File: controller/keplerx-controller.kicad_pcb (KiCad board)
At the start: 2 copper layers, 90 x 50 mm, 21 parts, among them J1 Conn_02x05_Odd_Even, J2 Conn_01x04, J3 Conn_01x04, SW1 Synth, SW2 ROM, SW3 Vol-, SW4 Vol+, SW5 RotaryEncoder_Switch

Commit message: 再再度出し直し(v2.0.2)
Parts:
- added H5: MountingHole_Pad, MountingHole:MountingHole_2.2mm_M2_ISO7380_Pad, F.Cu at (124.5, 99.5)
- added H6: MountingHole_Pad, MountingHole:MountingHole_2.2mm_M2_ISO7380_Pad, F.Cu at (124.5, 77.5)
- added H7: MountingHole_Pad, MountingHole:MountingHole_2.2mm_M2_ISO7380_Pad, F.Cu at (145.5, 99.5)
- added H8: MountingHole_Pad, MountingHole:MountingHole_2.2mm_M2_ISO7380_Pad, F.Cu at (145.5, 77.5)
- moved JP1 0.29 mm to (130.8, 73.3)
- moved JP4 0.24 mm to (130.8, 80.6)
- moved JP2 0.22 mm to (134.0, 73.3)
- moved JP3 0.15 mm to (134.0, 80.6)
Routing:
- net /BTN4: track 57.9 -> 56.4 mm
- net Net-(J3-Pad4): track 5.85 -> 5.33 mm
- net (no net): vias 4 -> 0
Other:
- board text added: "Developed by @kunichiko. January 2023 (V1.0.0)"
- board text added: "Kepler-X Controller"

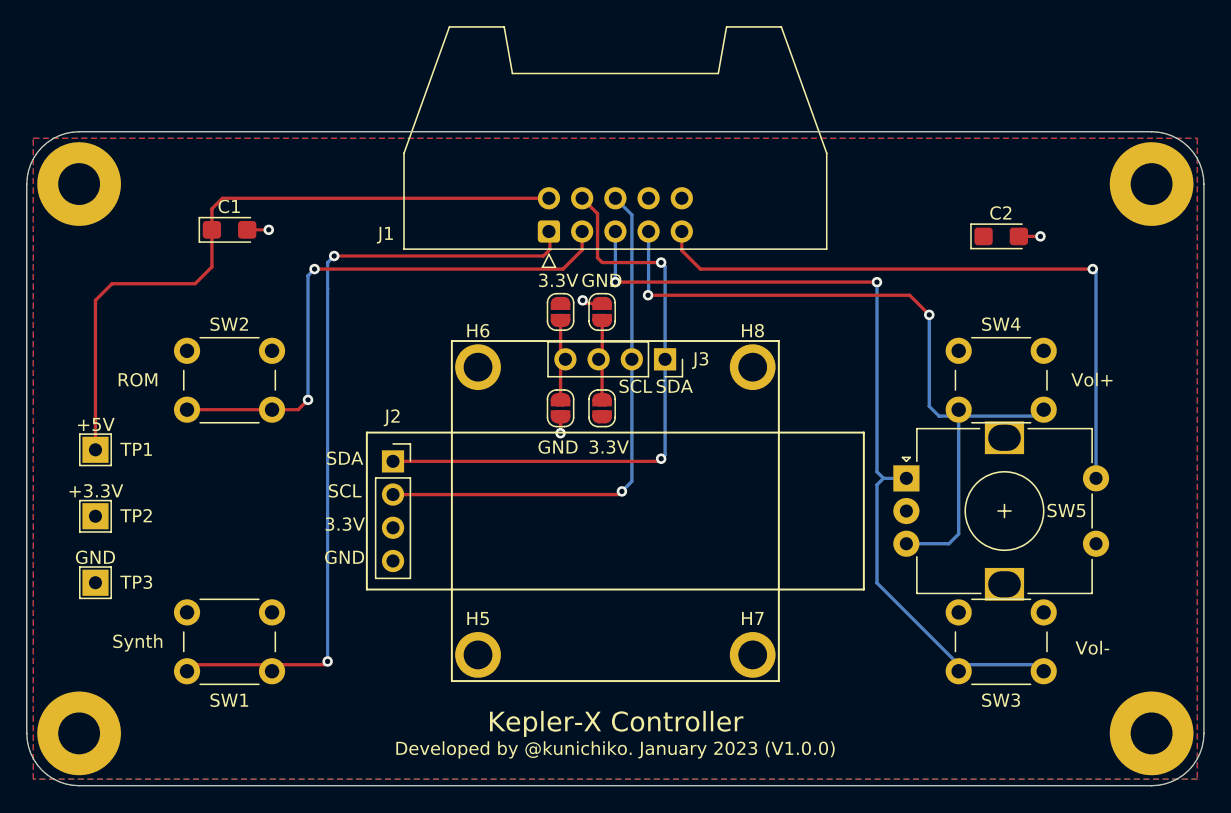
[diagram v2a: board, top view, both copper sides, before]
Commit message: v1.0.1 - Changed one of the two sets of open jumper pairs to a bridged jumper
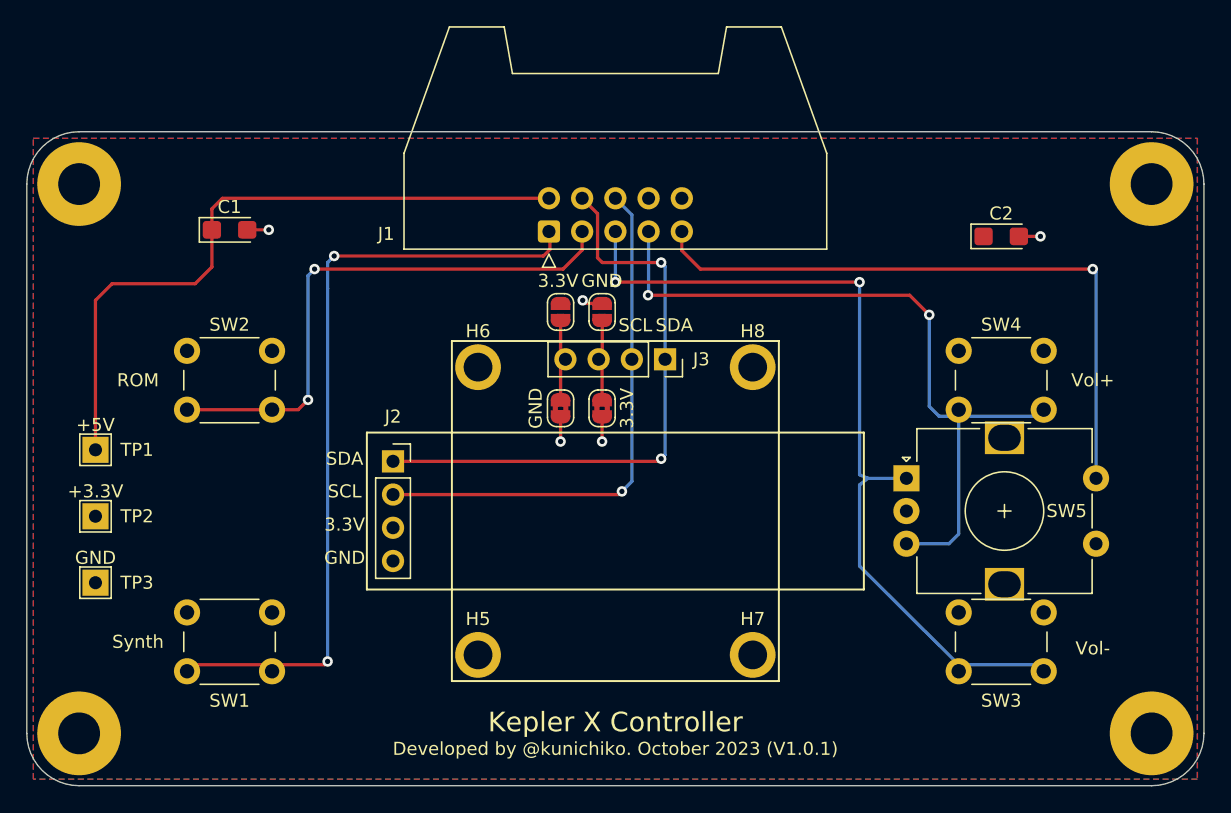
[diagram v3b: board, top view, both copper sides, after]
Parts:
- removed JP3: 3.3V, Jumper:SolderJumper-2_P1.3mm_Open_RoundedPad1.0x1.5mm
- removed JP4: GND, Jumper:SolderJumper-2_P1.3mm_Open_RoundedPad1.0x1.5mm
- added 3.3V: 3.3V, Jumper:SolderJumper-2_P1.3mm_Bridged2Bar_RoundedPad1.0x1.5mm, F.Cu at (134.0, 80.6)
- added GND: GND, Jumper:SolderJumper-2_P1.3mm_Bridged2Bar_RoundedPad1.0x1.5mm, F.Cu at (130.8, 80.6)
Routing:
- net /+3.3V: track 0.00 -> 1.89 mm, vias 0 -> 1
- net /BTN3: track 64.4 -> 65.1 mm
- net GND: track 6.14 -> 6.77 mm
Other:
- board text added: "Developed by @kunichiko. October 2023 (V1.0.1)"
- board text added: "Kepler X Controller"
- board text removed: "Developed by @kunichiko. January 2023 (V1.0.0)"
- board text removed: "Kepler-X Controller"
